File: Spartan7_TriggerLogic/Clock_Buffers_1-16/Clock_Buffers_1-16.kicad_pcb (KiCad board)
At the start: 4 copper layers, 38 parts, among them J1 Out_1, J10 Out_10, J11 Out_11, J12 Out_12, J13 Out_13, J14 Out_14, J15 Out_15, J16 Out_16, J17 CLK_In, J2 Out_2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

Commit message: .
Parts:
- added C201: 10uF, Capacitor_SMD:C_0805_2012Metric, F.Cu at (143.9, 95.4)
- added C202: 10p, Capacitor_SMD:C_0603_1608Metric, F.Cu at (152.0, 91.7)
- added C203: 10uF, Capacitor_SMD:C_0805_2012Metric, F.Cu at (151.5, 97.2)
- added D101: 5V, LED_SMD:LED_0603_1608Metric, F.Cu at (142.8, 91.9)
- added D102: 3V3, LED_SMD:LED_0603_1608Metric, F.Cu at (147.9, 91.9)
- added H1: fi_2.6mm, MountingHole:MountingHole_2.7mm_M2.5_Pad_Via, F.Cu at (106.9, 77.8)
- added H2: fi_2.6mm, MountingHole:MountingHole_2.7mm_M2.5_Pad_Via, F.Cu at (162.5, 77.8)
- added H3: fi_2.6mm, MountingHole:MountingHole_2.7mm_M2.5_Pad_Via, F.Cu at (106.9, 97.8)
- added H4: fi_2.6mm, MountingHole:MountingHole_2.7mm_M2.5_Pad_Via, F.Cu at (162.5, 97.8)
- added J18: USB_C_Receptacle_PowerOnly_6P, 0_lib:CONN6_USB4125_GCT, F.Cu at (120.8, 99.1)
- added J19: Soldarable pads, Connector_PinHeader_2.00mm:PinHeader_1x02_P2.00mm_Horizontal, F.Cu at (156.9, 97.5)
- added R101: 5k1, Resistor_SMD:R_0402_1005Metric, F.Cu at (141.5, 92.4)
- added R102: 5k1, Resistor_SMD:R_0402_1005Metric, F.Cu at (146.6, 92.4)
- added R19: 5k1, Resistor_SMD:R_0402_1005Metric, F.Cu at (121.3, 93.5)
- added R20: 5k1, Resistor_SMD:R_0402_1005Metric, F.Cu at (120.3, 93.5)
- added R201: 40k, Resistor_SMD:R_0603_1608Metric, F.Cu at (152.0, 93.2)
- added R202: 40k, Resistor_SMD:R_0603_1608Metric, F.Cu at (152.0, 94.7)
- added U201: LT3081EDF-TRPBF, 0_lib:DFN-12_DF_LIT, F.Cu at (147.6, 96.0)
- J10, J11, J12, J13, J14, J15, J6, J9: moved to B.Cu
- moved J16 101.7 mm to (160.1, 67.7), turned to 180 degrees
- moved J1 98.7 mm to (138.3, 67.7), turned to 180 degrees
- moved J2 96.8 mm to (145.6, 67.7), turned to 180 degrees
- moved J3 95.8 mm to (152.8, 67.7), turned to 180 degrees
- moved J6 90.6 mm to (138.3, 67.7)
- moved J9 87.7 mm to (160.1, 67.7)
- moved J12 84.2 mm to (145.6, 67.7)
- moved J13 83.3 mm to (152.8, 67.7)
- moved J10 79.2 mm to (123.8, 67.7)
- moved J11 78.2 mm to (131.1, 67.7)
- moved J14 77.1 mm to (116.5, 67.7)
- moved J4 65.8 mm to (131.1, 67.7), turned to 180 degrees
- moved J15 63.9 mm to (109.3, 67.7)
- moved J7 54.1 mm to (109.3, 67.7), turned to 180 degrees
- moved J8 53.1 mm to (116.5, 67.7), turned to 180 degrees
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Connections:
- J1 pad 1: /out_1 -> /out_8
- J10 pad 1: /out_10 -> /out_9
- J11 pad 1: /out_11 -> /out_10
- J12 pad 1: /out_12 -> /out_6
- J13 pad 1: /out_13 -> /out_4
- J14 pad 1: /out_14 -> /out_13
- J16 pad 1: /out_16 -> /out_3
- J2 pad 1: /out_2 -> /out_5
- J3 pad 1: /out_3 -> /out_1
- J4 pad 1: /out_4 -> /out_11
- J5 pad 1: /out_5 -> /out_12
- J6 pad 1: /out_6 -> /out_7
- J7 pad 1: /out_7 -> /out_16
- J8 pad 1: /out_8 -> /out_14
- J9 pad 1: /out_9 -> /out_2
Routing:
- net /5V_to_3V3/V_in: track 0.00 -> 44.7 mm, vias 0 -> 9
- net /out_2: track 0.00 -> 24.2 mm, vias 0 -> 1
- net /out_15: track 0.00 -> 24.0 mm, vias 0 -> 1
- net /out_4: track 0.00 -> 23.9 mm, vias 0 -> 1
- net /out_13: track 0.00 -> 22.6 mm, vias 0 -> 1
- net /out_12: track 0.00 -> 21.4 mm
- net /out_16: track 0.00 -> 21.2 mm
- net /out_1: track 0.00 -> 21.0 mm
- net /out_3: track 0.00 -> 20.4 mm
- net /out_14: track 0.00 -> 20.0 mm
- net /out_5: track 0.00 -> 19.9 mm
- net /out_9: track 0.00 -> 19.8 mm, vias 0 -> 1
- net /out_6: track 0.00 -> 18.1 mm, vias 0 -> 1
- net /out_7: track 0.00 -> 17.3 mm, vias 0 -> 1
- net /out_10: track 0.00 -> 17.1 mm, vias 0 -> 1
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- added copper zone on F.Cu, net /5V_to_3V3/V_in
- added copper zone on B.Cu, net GND
- added copper zone on F.Cu, net GND
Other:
- board outline added: 63 x 37.8 mm
- board text added: "16 Channels Clock Buffer Rev_0 August 2025 TU Darmstadt"
- board text added: "3V3"
- board text added: "5V"
- board text added: "Designed by A. Enciu"

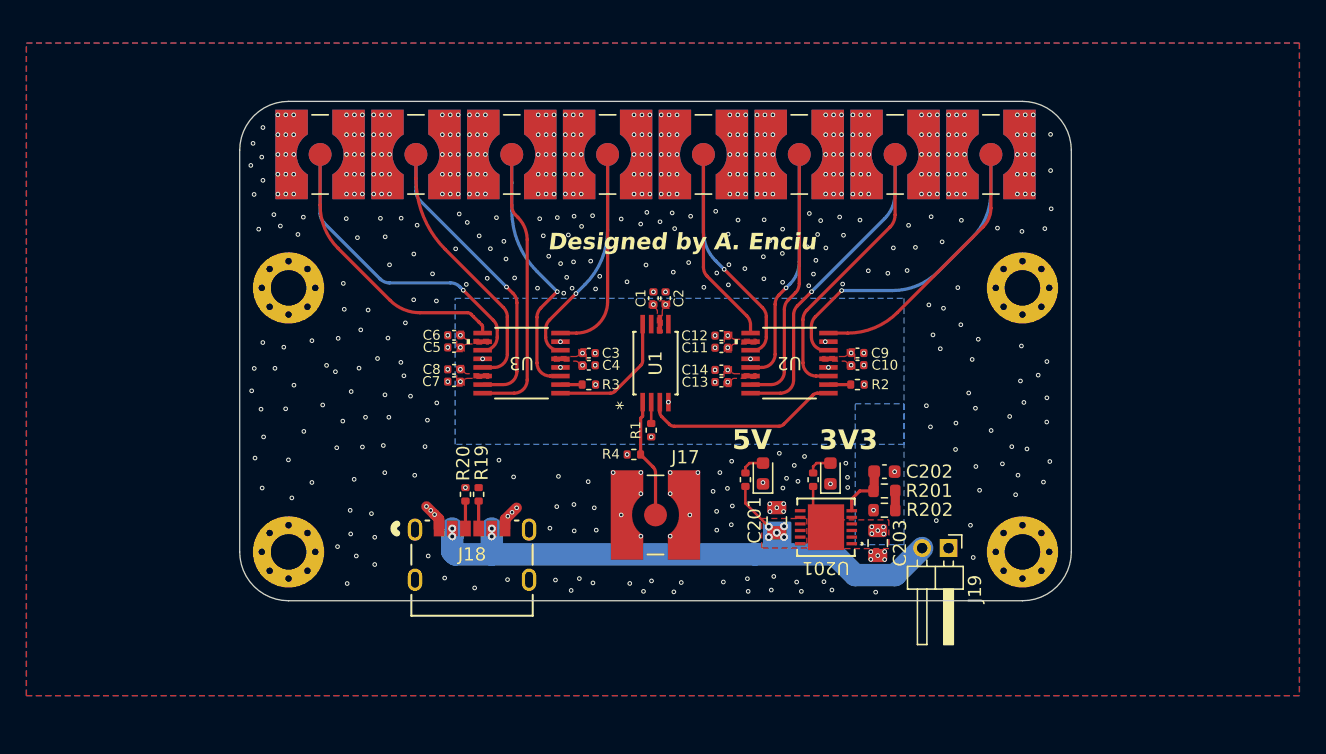
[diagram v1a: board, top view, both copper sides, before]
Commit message: Update PCB layout and add new backup and SPICE files
Added new backup ZIP files and SPICE simulation files for Clock_Buffers_1-16 and HYDRA_VMM3_CARD_V3_Flex, while removing outdated backup files. Updated multiple footprints and component placements in Clock_Buffers_1-16.kicad_pcb, reflecting changes in component positions and orientations. Minor update to .kicad_prl files to reflect active layer changes.
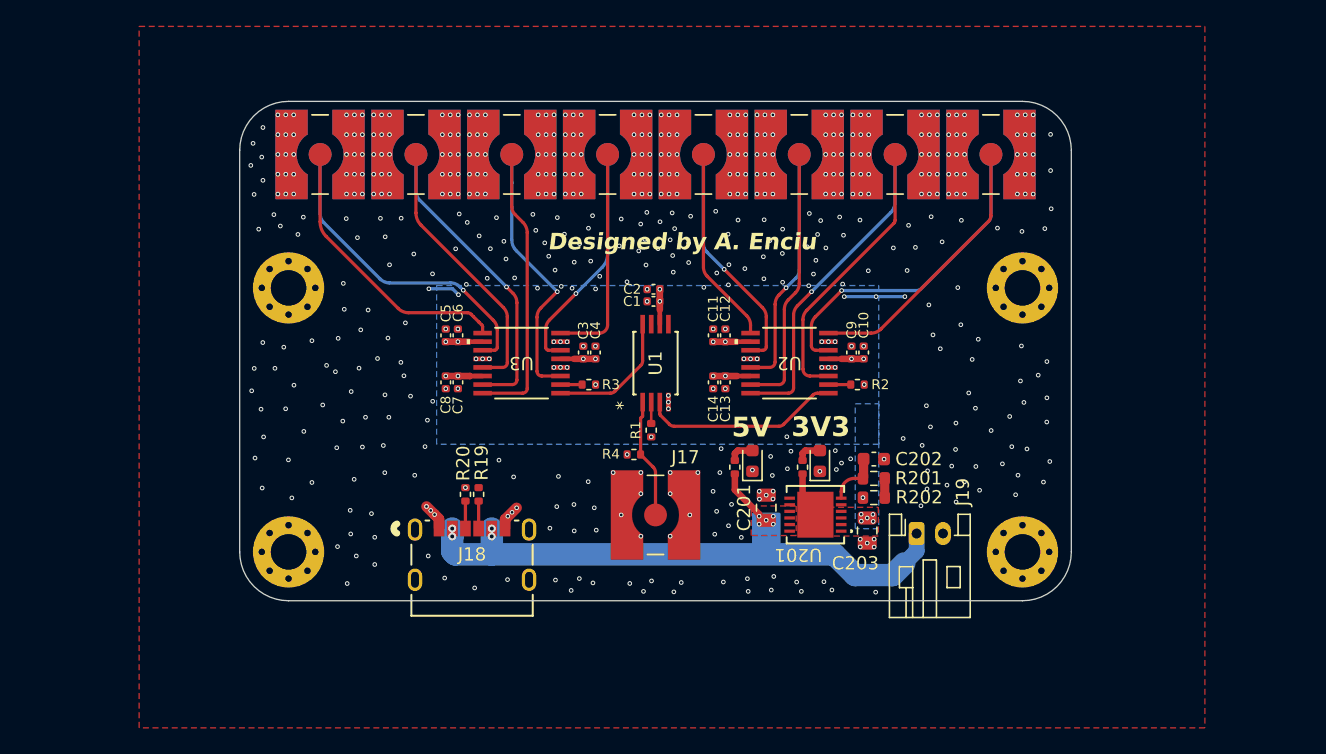
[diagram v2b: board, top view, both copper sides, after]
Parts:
- J19: footprint Connector_PinHeader_2.00mm:PinHeader_1x02_P2.00mm_Horizontal -> Connector_JST:JST_PH_S2B-PH-K_1x02_P2.00mm_Horizontal
- moved J19 2.66 mm to (154.5, 96.4), turned to 0 degrees
- moved C201 1.24 mm to (143.1, 94.5)
- moved U201 1.24 mm to (146.8, 95.0)
- moved D101 1.24 mm to (142.0, 90.9)
- moved C203 1.24 mm to (150.7, 96.2)
- moved R201 1.24 mm to (151.2, 92.2)
- moved R202 1.24 mm to (151.2, 93.7)
- moved C202 1.24 mm to (151.2, 90.8)
- moved D102 1.24 mm to (147.2, 90.9)
- moved R101 1.24 mm to (140.7, 91.4)
- moved R102 1.24 mm to (145.8, 91.4)
- moved C8 1.17 mm to (118.8, 85.0), turned to -90 degrees
- moved C2 1.14 mm to (134.5, 77.9), turned to 180 degrees
- moved C14 1.13 mm to (139.1, 85.0), turned to -90 degrees
- moved C11 1.12 mm to (139.1, 81.4), turned to 90 degrees
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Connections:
- J19 pad 1: GND -> /5V_to_3V3/V_in
- J19 pad 2: /5V_to_3V3/V_in -> GND
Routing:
- net +3V3: track 3.40 -> 22.9 mm
- net GND: track 4.00 -> 11.0 mm, vias 534 -> 561
- net /5V_to_3V3/V_in: track 44.7 -> 45.7 mm
- net /out_11: track 16.0 -> 16.8 mm
- net /out_2: track 24.2 -> 24.9 mm
- net /out_14: track 20.0 -> 20.6 mm
- net /out_10: track 17.1 -> 17.7 mm
- net /out_9: track 19.8 -> 20.4 mm
- removed copper zone on B.Cu, net GND

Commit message: .
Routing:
- removed copper zone on F.Cu, net GND
